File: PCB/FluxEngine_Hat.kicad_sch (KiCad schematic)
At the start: 6 parts, among them J1 Conn_01x26, J2 Conn_01x26, J3 Conn_01x03, J4 FDD_PC34_host, J5 FDD_Shugart50_host

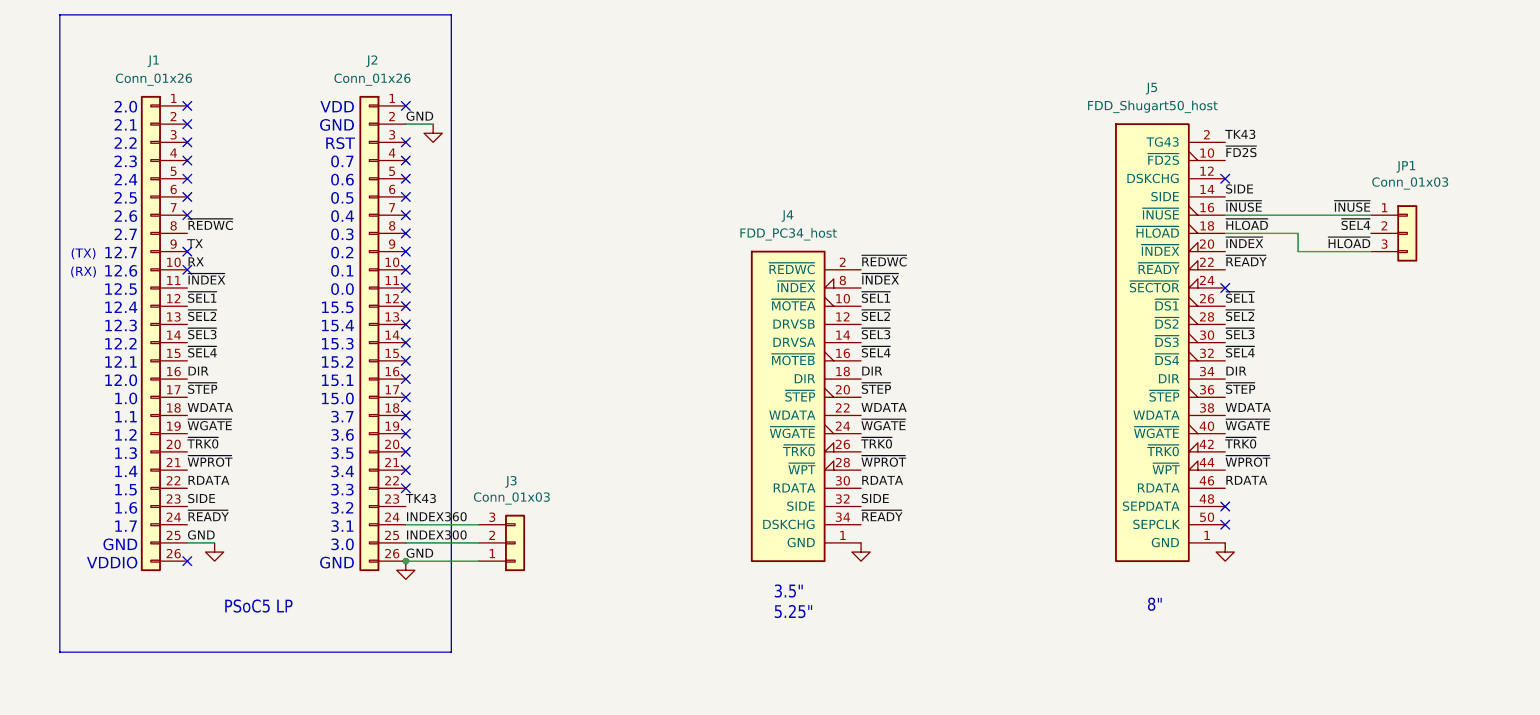
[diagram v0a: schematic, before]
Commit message: v003 flip fpga board over
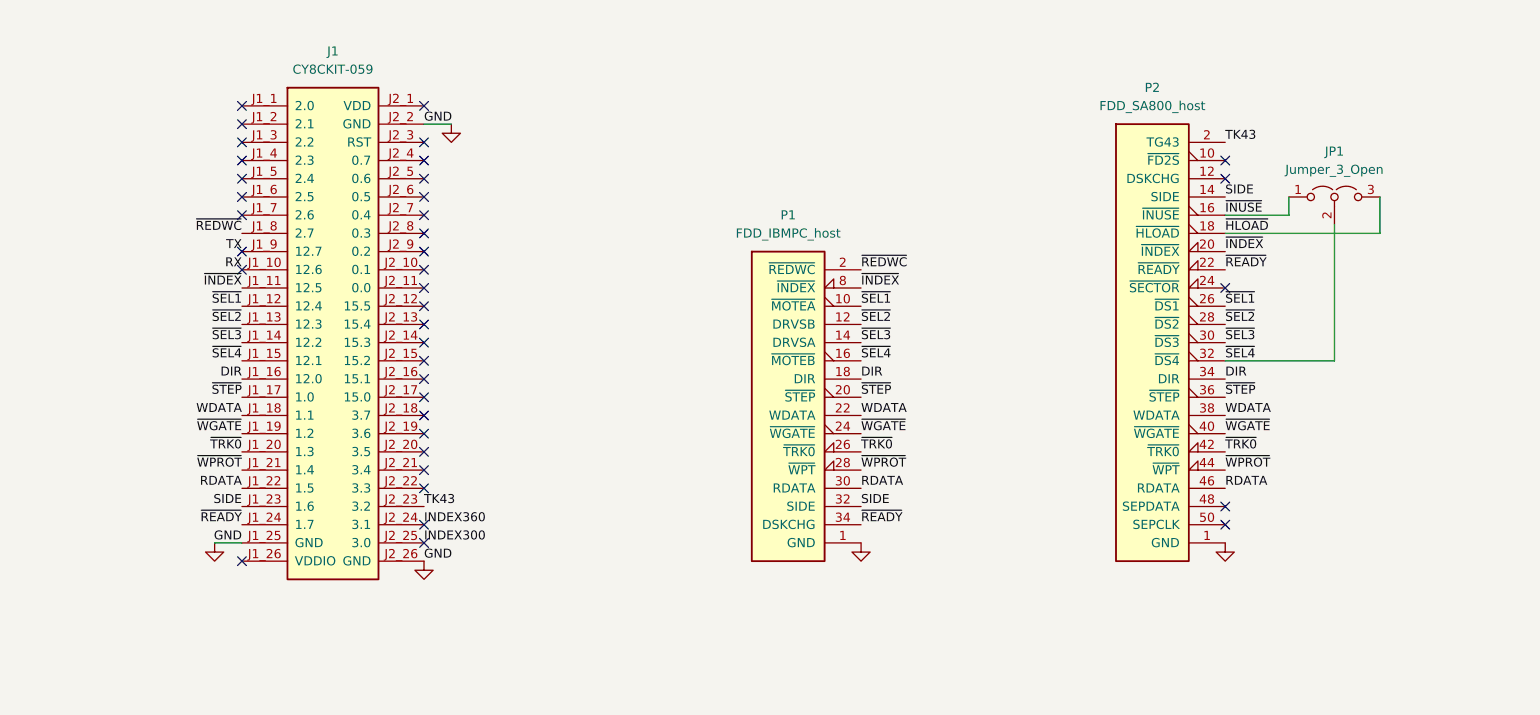
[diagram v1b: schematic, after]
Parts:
- removed J1, J2: Conn_01x26, 000_LOCAL:PinHeader_1x26_P2.54mm_Vertical, symbol 000_LOCAL:Conn_01x26
- removed J3, JP1: Conn_01x03, 000_LOCAL:PinHeader_1x03_P2.54mm_Vertical, symbol 000_LOCAL:Conn_01x03
- removed J4: FDD_PC34_host, 000_LOCAL:IDC-Header_2x17_P2.54mm_Latch_Vertical - FDD, symbol 000_LOCAL:FDD_PC34_host
- removed J5: FDD_Shugart50_host, 000_LOCAL:IDC-Header_2x25_P2.54mm_Latch_Vertical, symbol 000_LOCAL:FDD_Shugart50_host
- added J1: CY8CKIT-059, 000_LOCAL:CY8CKIT-059, symbol 000_LOCAL:CY8CKIT-059
- added JP1: Jumper_3_Open, 000_LOCAL:PinHeader_1x03_P2.54mm_Vertical bare, symbol 000_LOCAL:Jumper_3_Open
- added P1: FDD_IBMPC_host, 000_LOCAL:IDC-Header_2x17_P2.54mm_Latch_Vertical - FDD, symbol 000_LOCAL:FDD_IBMPC_host
- added P2: FDD_SA800_host, 000_LOCAL:IDC-Header_2x25_P2.54mm_Latch_Vertical, symbol 000_LOCAL:FDD_SA800_host
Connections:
- net DIR: now also J1.J1_16 (12.0), P1.18 (DIR), P2.34 (DIR)
- net GND: now also J1.J1_25 (GND), J1.J2_2 (GND), J1.J2_26 (GND), P1.1 (GND), P1.11 (GND), P1.13 (GND), P1.15 (GND), P1.17 (GND), P1.19 (GND), P1.21 (GND), P1.23 (GND), P1.25 (GND), P1.27 (GND), P1.29 (GND), P1.31 (GND), P1.33 (GND), P1.7 (GND), P1.9 (GND), P2.1 (GND), P2.11 (GND), P2.13 (GND), P2.15 (GND), P2.17 (GND), P2.19 (GND), P2.21 (GND), P2.23 (GND), P2.25 (GND), P2.27 (GND), P2.29 (GND), P2.3 (GND), P2.31 (GND), P2.33 (GND), P2.35 (GND), P2.37 (GND), P2.39 (GND), P2.41 (GND), P2.43 (GND), P2.45 (GND), P2.47 (GND), P2.49 (GND), P2.5 (GND), P2.7 (GND), P2.9 (GND)
- net INDEX300: now also J1.J2_25 (3.0)
- net INDEX360: now also J1.J2_24 (3.1)
- net RDATA: now also J1.J1_22 (1.5), P1.30 (RDATA), P2.46 (RDATA)
- net RX: now also J1.J1_10 (12.6)
- net SIDE: now also J1.J1_23 (1.6), P1.32 (SIDE), P2.14 (SIDE)
- net TK43: now also J1.J2_23 (3.2), P2.2 (TG43)
- net TX: now also J1.J1_9 (12.7)
- net WDATA: now also J1.J1_18 (1.1), P1.22 (WDATA), P2.38 (WDATA)
- net ~{HLOAD}: now also JP1.3 (B), P2.18 (~{HLOAD})
- net ~{INDEX}: now also J1.J1_11 (12.5), P1.8 (~{INDEX}), P2.20 (~{INDEX})
- net ~{INUSE}: now also JP1.1 (A), P2.16 (~{INUSE})
- net ~{READY}: now also J1.J1_24 (1.7), P1.34 (DSKCHG), P2.22 (~{READY})
- net ~{REDWC}: now also J1.J1_8 (2.7), P1.2 (~{REDWC})
- net ~{SEL1}: now also J1.J1_12 (12.4), P1.10 (~{MOTEA}), P2.26 (~{DS1})
- net ~{SEL2}: now also J1.J1_13 (12.3), P1.12 (DRVSB), P2.28 (~{DS2})
- net ~{SEL3}: now also J1.J1_14 (12.2), P1.14 (DRVSA), P2.30 (~{DS3})
- net ~{SEL4}: now also J1.J1_15 (12.1), JP1.2 (C), P1.16 (~{MOTEB}), P2.32 (~{DS4})
- net ~{STEP}: now also J1.J1_17 (1.0), P1.20 (~{STEP}), P2.36 (~{STEP})
- net ~{TRK0}: now also J1.J1_20 (1.3), P1.26 (~{TRK0}), P2.42 (~{TRK0})
- net ~{WGATE}: now also J1.J1_19 (1.2), P1.24 (~{WGATE}), P2.40 (~{WGATE})
- net ~{WPROT}: now also J1.J1_21 (1.4), P1.28 (~{WPT}), P2.44 (~{WPT})
- no-connect marks 35 -> 38
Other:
- note removed: "(RX)"
- note removed: "(TX)"
- note removed: "2.0 2.1 2.2 2.3 2.4 2.5 2.6 2.7 12.7 12.6 12.5 12.4 12.3 12.2 12.1 12.0 1.0 1.1 1.2 1.3 1.4 1.5 1.6 1.7 GND VDDIO"
- note removed: "3.5" 5.25""
- note removed: "8""
- note removed: "PSoC5 LP"
- note removed: "VDD GND RST 0.7 0.6 0.5 0.4 0.3 0.2 0.1 0.0 15.5 15.4 15.3 15.2 15.1 15.0 3.7 3.6 3.5 3.4 3.3 3.2 3.1 3.0 GND"

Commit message: jumper options and printable case
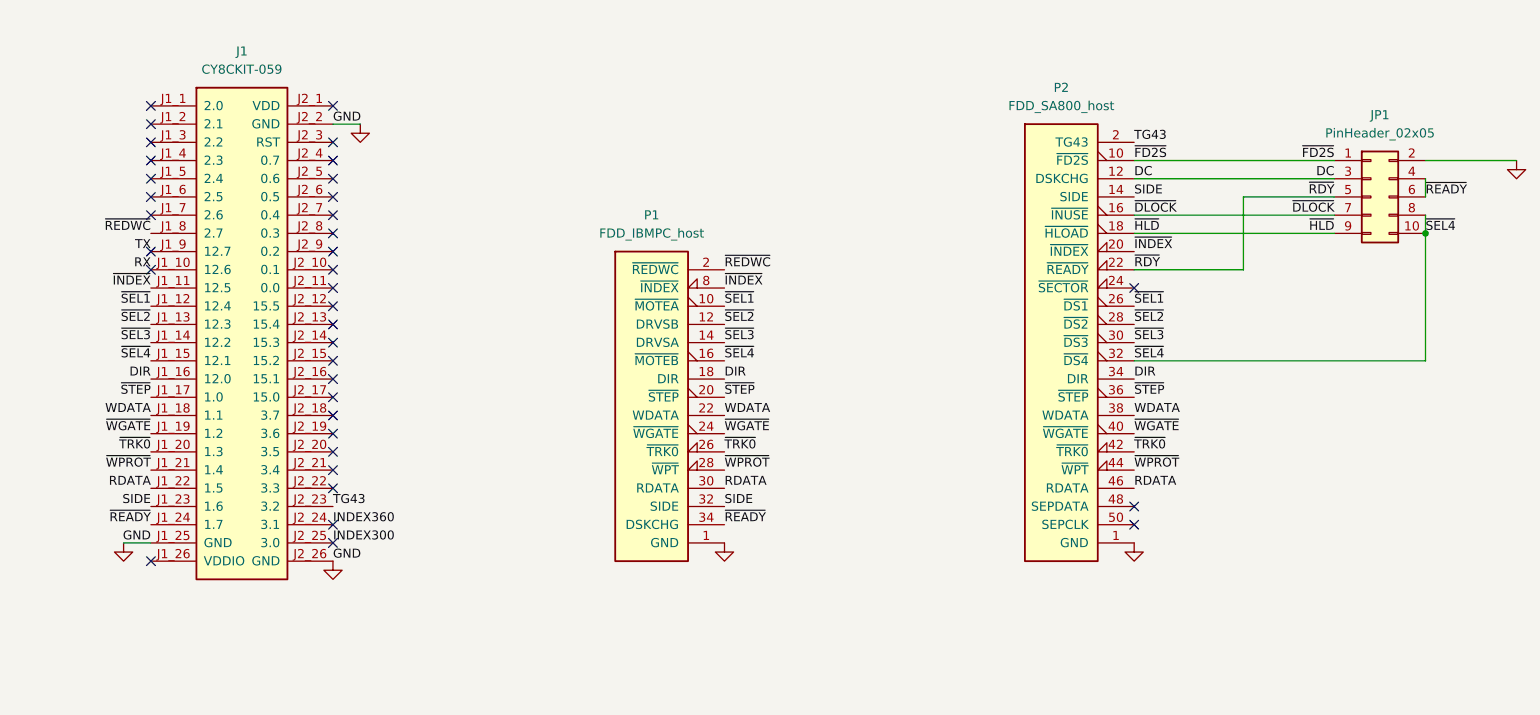
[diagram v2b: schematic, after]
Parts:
- removed JP1: Jumper_3_Open, 000_LOCAL:PinHeader_1x03_P2.54mm_Vertical bare, symbol 000_LOCAL:Jumper_3_Open
- added JP1: PinHeader_02x05, 000_LOCAL:PinHeader_2x05_P2.54mm_Vertical, symbol 000_LOCAL:Conn_02x05_Odd_Even
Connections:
- net GND: now also JP1.2 (Pin_2)
- net ~{READY}: now also JP1.4 (Pin_4), JP1.6 (Pin_6); no longer P2.22 (~{READY})
- net ~{SEL4}: now also JP1.10 (Pin_10), JP1.8 (Pin_8)
- net ~{FD2S}: now reaches P2.10 (~{FD2S})
- net ~{FD2S}: now also JP1.1 (Pin_1)
- net DC: now reaches P2.12 (DSKCHG)
- net DC: now also JP1.3 (Pin_3)
- net TK43 renamed TG43
- net ~{HLOAD} renamed ~{HLD}
- net ~{HLD}: now also JP1.9 (Pin_9)
- net ~{INUSE} renamed ~{DLOCK}
- net ~{DLOCK}: now also JP1.7 (Pin_7)
- new net ~{RDY}: JP1.5 (Pin_5), P2.22 (~{READY})
- no-connect marks 38 -> 36
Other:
- moved on the sheet: J1, P1, P2

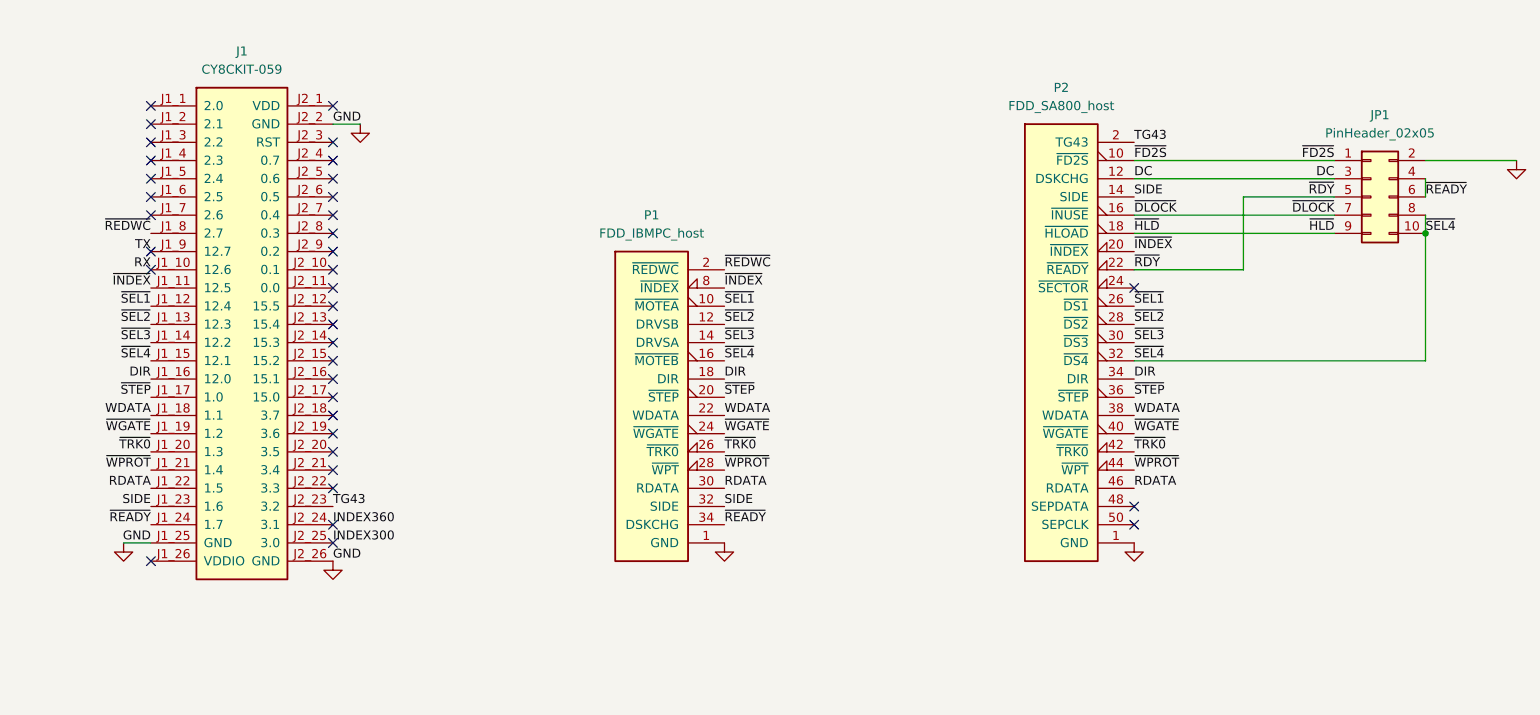
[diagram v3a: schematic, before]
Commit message: better jumper arrangement, fix some signal names
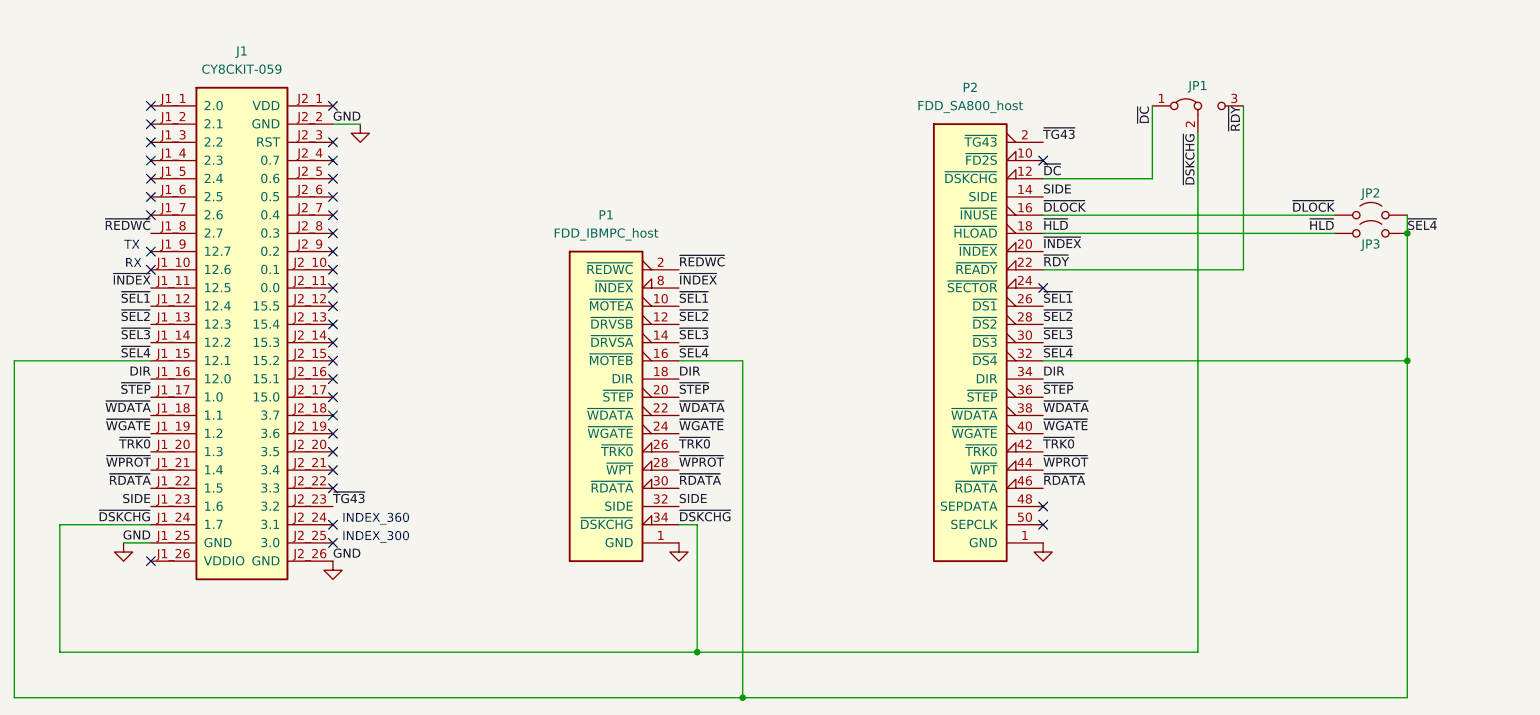
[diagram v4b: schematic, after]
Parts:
- removed JP1: PinHeader_02x05, 000_LOCAL:PinHeader_2x05_P2.54mm_Vertical, symbol 000_LOCAL:Conn_02x05_Odd_Even
- added JP1: Jumper_3_Bridged12, 000_LOCAL:PinHeader_1x03_P2.54mm_Vertical, symbol 000_LOCAL:Jumper_3_Bridged12
- added JP2, JP3: Jumper_2_Open, 000_LOCAL:PinHeader_1x02_P2.54mm_Vertical, symbol 000_LOCAL:Jumper_2_Open
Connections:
- net ~{DLOCK}: now also JP2.1 (A)
- net ~{HLD}: now also JP3.1 (A)
- net ~{RDY}: now also JP1.3 (B)
- net ~{SEL4}: now also JP2.2 (B), JP3.2 (B)
- net DC renamed ~{DC}
- net ~{DC}: now also JP1.1 (A)
- net INDEX300: no longer names the net of J1.J2_25 (3.0)
- net INDEX360: no longer names the net of J1.J2_24 (3.1)
- net RDATA renamed ~{RDATA}
- net RX: no longer names the net of J1.J1_10 (12.6)
- net TG43 renamed ~{TG43}
- net TX: no longer names the net of J1.J1_9 (12.7)
- net WDATA renamed ~{WDATA}
- net ~{FD2S}: no longer names the net of P2.10 (~{FD2S})
- net ~{READY} renamed ~{DSKCHG}
- net ~{DSKCHG}: now also JP1.2 (C)
- no-connect marks 36 -> 37
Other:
- note added: "INDEX_300"
- note added: "INDEX_360"
- note added: "RX"
- note added: "TX"

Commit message: solderless pins footprint, add simple cover for solderless and sockets
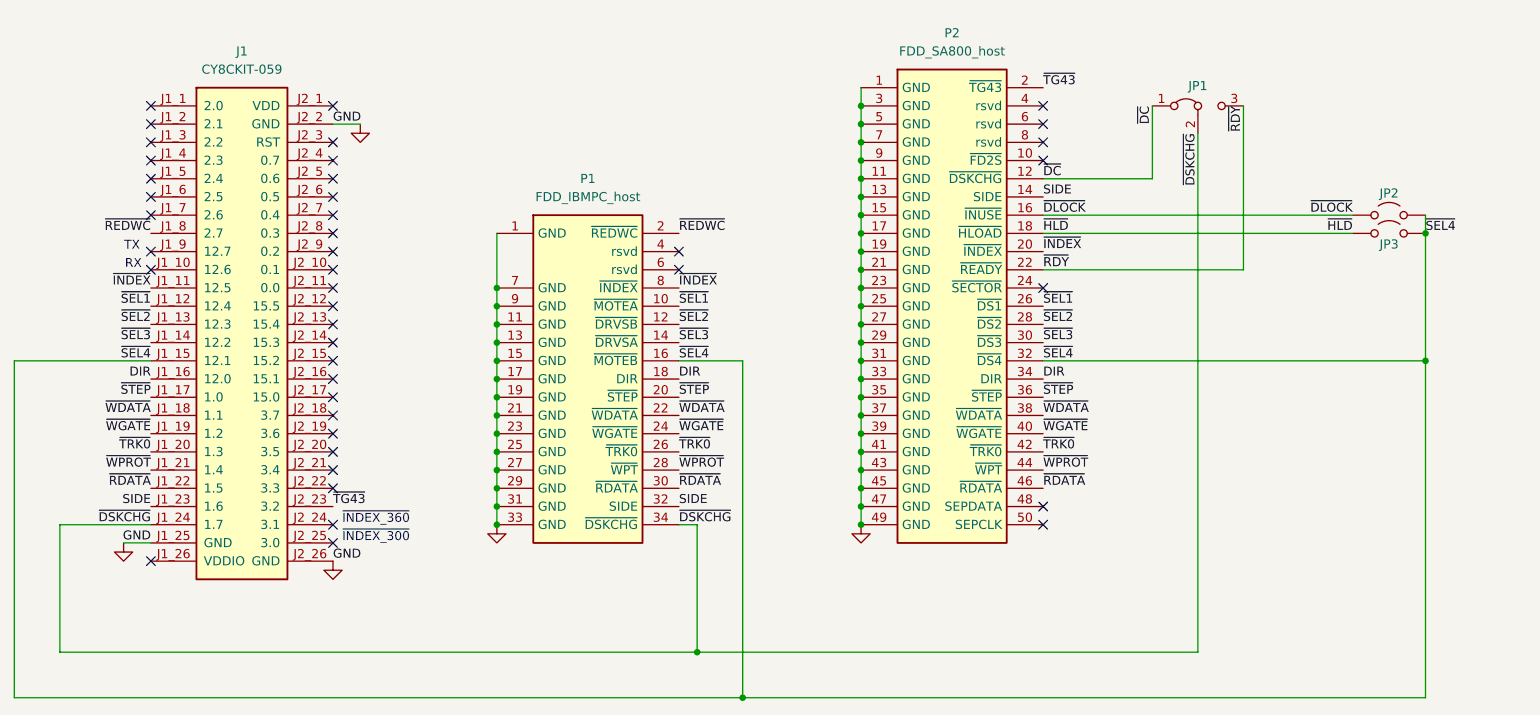
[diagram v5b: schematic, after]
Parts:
- J1: footprint 000_LOCAL:CY8CKIT-059 -> 000_LOCAL:CY8CKIT-059 dry fit
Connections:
- no-connect marks 37 -> 42
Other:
- note added: "~{INDEX_300}"
- note added: "~{INDEX_360}"
- note removed: "INDEX_300"
- note removed: "INDEX_360"
- moved on the sheet: JP2, JP3
